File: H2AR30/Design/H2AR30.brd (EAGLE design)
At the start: 34.6 x 30 mm, 59 parts, among them P1 HEXABIT_17.32, U2 INA199A2DCKT, U3 INA199A2DCKT, U4 TEXAS_INSTRUMENTS_REF3212AIDB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, X1 XTALL_CSTCE8M00G52

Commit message: some bugs fixed
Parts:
- U2, U3: value INA199A2DCKT -> INA199B2DCKT
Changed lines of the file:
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@@
 <attribute name="VALUE" x="6.26" y="-27.758" size="1.016" layer="27"/>
 </element>
-<element name="U2" library="HEXABITZ_ICs" library_urn="urn:adsk.eagle:library:20064554" package="SOT65P210X110-6N" package3d_urn="urn:adsk.eagle:package:19904117/2" value="INA199A2DCKT" x="9.906" y="-32.512" smashed="yes">
+<element name="U2" library="HEXABITZ_ICs" library_urn="urn:adsk.eagle:library:20064554" package="SOT65P210X110-6N" package3d_urn="urn:adsk.eagle:package:19904117/2" value="INA199B2DCKT" x="9.906" y="-32.512" smashed="yes">
 <attribute name="DESCRIPTION" value="26V, bi-directional current sense amplifier 6-SC70 -40 to 125" x="9.906" y="-32.512" size="1.778" layer="27" display="off"/>
 <attribute name="MFN" value="Texas Instruments" x="9.906" y="-32.512" size="1.778" layer="27" display="off"/>
-<attribute name="MPN" value="INA199A2DCKT" x="9.906" y="-32.512" size="1.778" layer="27" display="off"/>
+<attribute name="MPN" value="INA199B2DCKT" x="9.906" y="-32.512" size="1.778" layer="27" display="off"/>
 <attribute name="NAME" x="6.4516" y="-29.972" size="2.0828" layer="25" ratio="10" rot="SR0"/>
-<attribute name="OCTOPART_URL" value="https://octopart.com/ina199a2dckt-texas+instruments-18607270?r=sp" x="9.906" y="-32.512" size="1.778" layer="27" display="off"/>
+<attribute name="OCTOPART_URL" value="https://octopart.com/ina199b2dckt-texas+instruments-24258237?r=sp" x="9.906" y="-32.512" size="1.778" layer="27" display="off"/>
 <attribute name="VALUE" x="6.4516" y="-36.957" size="2.0828" layer="27" ratio="10" rot="SR0"/>
 </element>
@@
 <attribute name="VALUE" x="6.985" y="-108.839" size="1.27" layer="27"/>
 </element>
-<element name="U3" library="HEXABITZ_ICs" library_urn="urn:adsk.eagle:library:20064554" package="SOT65P210X110-6N" package3d_urn="urn:adsk.eagle:package:19904117/2" value="INA199A2DCKT" x="9.906" y="-112.903" smashed="yes">
+<element name="U3" library="HEXABITZ_ICs" library_urn="urn:adsk.eagle:library:20064554" package="SOT65P210X110-6N" package3d_urn="urn:adsk.eagle:package:19904117/2" value="INA199B2DCKT" x="9.906" y="-112.903" smashed="yes">
 <attribute name="DESCRIPTION" value="26V, bi-directional current sense amplifier 6-SC70 -40 to 125" x="9.906" y="-112.903" size="1.778" layer="27" display="off"/>
 <attribute name="MFN" value="Texas Instruments" x="9.906" y="-112.903" size="1.778" layer="27" display="off"/>
-<attribute name="MPN" value="INA199A2DCKT" x="9.906" y="-112.903" size="1.778" layer="27" display="off"/>
+<attribute name="MPN" value="INA199B2DCKT" x="9.906" y="-112.903" size="1.778" layer="27" display="off"/>
 <attribute name="NAME" x="6.4516" y="-110.363" size="2.0828" layer="25" ratio="10" rot="SR0"/>
-<attribute name="OCTOPART_URL" value="https://octopart.com/ina199a2dckt-texas+instruments-18607270?r=sp" x="9.906" y="-112.903" size="1.778" layer="27" display="off"/>
+<attribute name="OCTOPART_URL" value="https://octopart.com/ina199b2dckt-texas+instruments-24258237?r=sp" x="9.906" y="-112.903" size="1.778" layer="27" display="off"/>
 <attribute name="VALUE" x="6.4516" y="-117.348" size="2.0828" layer="27" ratio="10" rot="SR0"/>
 </element>

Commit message: some fixes
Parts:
- R10, R9: value 330k -> 1M
- R8: value 330K -> 1M
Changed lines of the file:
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@@
 <attribute name="VALUE" x="6.731" y="-94.234" size="1.27" layer="27"/>
 </element>
-<element name="R8" library="HEXABITZ_RCLS" library_urn="urn:adsk.eagle:library:20064561" package="R1206" package3d_urn="urn:adsk.eagle:package:23540/2" value="330K" x="8.255" y="-97.917" smashed="yes">
+<element name="R8" library="HEXABITZ_RCLS" library_urn="urn:adsk.eagle:library:20064561" package="R1206" package3d_urn="urn:adsk.eagle:package:23540/2" value="1M" x="8.255" y="-97.917" smashed="yes">
 <attribute name="NAME" x="6.985" y="-96.647" size="1.27" layer="25"/>
 <attribute name="POPULARITY" value="19" x="8.255" y="-97.917" size="1.778" layer="27" display="off"/>
@@
 <attribute name="VALUE" x="6.985" y="-100.457" size="1.27" layer="27"/>
 </element>
-<element name="R9" library="HEXABITZ_RCLS" library_urn="urn:adsk.eagle:library:20064561" package="R1206" package3d_urn="urn:adsk.eagle:package:23540/2" value="330k" x="8.255" y="-102.108" smashed="yes">
+<element name="R9" library="HEXABITZ_RCLS" library_urn="urn:adsk.eagle:library:20064561" package="R1206" package3d_urn="urn:adsk.eagle:package:23540/2" value="1M" x="8.255" y="-102.108" smashed="yes">
 <attribute name="NAME" x="6.985" y="-100.838" size="1.27" layer="25"/>
 <attribute name="POPULARITY" value="19" x="8.255" y="-102.108" size="1.778" layer="27" display="off"/>
@@
 <attribute name="VALUE" x="6.985" y="-104.648" size="1.27" layer="27"/>
 </element>
-<element name="R10" library="HEXABITZ_RCLS" library_urn="urn:adsk.eagle:library:20064561" package="R1206" package3d_urn="urn:adsk.eagle:package:23540/2" value="330k" x="8.255" y="-106.299" smashed="yes">
+<element name="R10" library="HEXABITZ_RCLS" library_urn="urn:adsk.eagle:library:20064561" package="R1206" package3d_urn="urn:adsk.eagle:package:23540/2" value="1M" x="8.255" y="-106.299" smashed="yes">
 <attribute name="NAME" x="6.985" y="-105.029" size="1.27" layer="25"/>
 <attribute name="POPULARITY" value="19" x="8.255" y="-106.299" size="1.778" layer="27" display="off"/>

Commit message: no message
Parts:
- removed C13, C20: 1.00uF, HEXABITZ_RCLS:C-0805-POL
- P1: value HEXABIT_17.32 -> HEXABIT__NO_P1_P5_P6_P7_P12; device hexabitz_connectors:HEXABIT_17.32 -> hexabitz_connectors:HEXABIT_17.32_NO_P1_P6_P5_P7_P12
- R10, R8, R9: value 1M -> 1M0
- R11, R12, R4, R5: value 1.01R -> 1R0
- R14: value 3.3K -> 150R; device HEXABITZ_RCLS:R-0603 -> HEXABITZ_RCLS:R1206
- U3: value INA199B2DCKT -> INA199B1DCKT
- U4: value TEXAS_INSTRUMENTS_REF3212AIDBVRTEXAS_INSTRUMENTS_REF3212AIDBVR_0_0 -> TEXAS_INSTRUMENTS_REF2033AIDDCRTEXAS_INSTRUMENTS_REF2033AIDDCR_0_2; device HEXABITZ_ICs:TEXAS_INSTRUMENTS_REF3212AIDBVR_0 -> HEXABITZ_ICs:TEXAS_INSTRUMENTS_REF2033AIDDCR_2
- moved C24 207.7 mm to (34.7, 41.5), turned to 270 degrees
- moved R14 191.9 mm to (30.7, 44.5), flipped to the bottom, turned to 90 degrees
- moved C22 190.2 mm to (35.2, 33.4), turned to 270 degrees
- moved U4 186.4 mm to (34.7, 37.2), turned to 90 degrees
- moved C23 185.1 mm to (34.7, 23.7), turned to 180 degrees
- moved D3 184.1 mm to (32.0, 40.0), turned to 60 degrees
- moved R15 183.9 mm to (35.2, 30.2), turned to 270 degrees
- moved C21 162.3 mm to (27.9, 23.4), turned to 90 degrees
- moved R11 157.0 mm to (31.8, 29.6), turned to 270 degrees
- moved C18 156.4 mm to (27.9, 26.4), turned to 270 degrees
- moved R12 156.1 mm to (29.5, 29.6), turned to 270 degrees
- moved FB4 154.7 mm to (31.8, 33.3), turned to 270 degrees
- moved FB5 154.3 mm to (29.5, 33.3), turned to 270 degrees
- moved C19 153.0 mm to (24.8, 32.3), flipped to the bottom, turned to 270 degrees
- moved R10 152.9 mm to (33.7, 44.5), flipped to the bottom, turned to 90 degrees
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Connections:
- net N$13 renamed CURRENT_P
- net N$14 renamed CURRENT_N
- removed net USART1_RX: P1.PAD_PD5, U1.P$31
- removed net USART1_TX: P1.PAD_PU5, U1.P$30
- removed net USART4_RX: P1.PAD_PD1, U1.P$11
- removed net USART4_TX: P1.PAD_PU1, U1.P$10
- removed net VDDA: C1.1, C13.1, C14.1, C2.1, C20.1, C21.1, C24.1, FB1.1, U1.P$9
- removed net VSSA: C1.2, C13.2, C14.2, C2.2, C20.2, C21.2, C24.2, R2.2, U1.P$8
- net AGND: now also C1.2, C14.2, C2.2, C21.2, C24.2, R2.2, U1.P$8; no longer U4.1
- net CURRENT_SENSE: now also U1.P$17; no longer U1.P$29
- net GND: now also U1.P$2, U1.P$20, U1.P$27, U1.P$28, U1.P$3; no longer P1.PAD_PD12, P1.PAD_PD7
- net NEUTRAL: now also P2.1; no longer P2.2
- net PHASE: now also P2.2; no longer P2.1
- net USART5_RX: no longer P1.PAD_PD6
- net USART5_TX: no longer P1.PAD_PU6
- net VCC: now also C1.1, C14.1, C2.1, C21.1, C24.1, FB1.1, U1.P$9, U4.5
- net VDD: no longer P1.PAD_PU12, P1.PAD_PU7
- net VOLTAGE_SENSE: now also U1.P$29; no longer U1.P$17
- net V_REF: now also U4.1; no longer U4.5, U4.6
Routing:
- net VCC: track 0.00 -> 68.7 mm, vias 0 -> 3
- net AGND: track 0.00 -> 64.8 mm, vias 0 -> 6
- net V_REF: track 0.00 -> 22.8 mm, vias 0 -> 3
- net VDD: track 0.00 -> 18.0 mm, vias 0 -> 3
- net N$21: track 0.00 -> 16.7 mm, vias 0 -> 1
- net USART3_TX: track 0.00 -> 16.2 mm, vias 0 -> 1
- net NEUTRAL: track 0.00 -> 15.8 mm, vias 0 -> 1
- net USART3_RX: track 0.00 -> 15.8 mm
- net CT_1: track 0.00 -> 14.9 mm
- net B1: track 0.00 -> 14.4 mm, vias 0 -> 1
- net USART2_TX: track 0.00 -> 14.0 mm, vias 0 -> 1
- net USART6_TX: track 0.00 -> 13.1 mm, vias 0 -> 1
- net N$7: track 0.00 -> 13.0 mm, vias 0 -> 1
- net USART2_RX: track 0.00 -> 12.9 mm
- net N$3: track 0.00 -> 12.7 mm, vias 0 -> 1
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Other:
- board text added: "CT1"
- board text added: "CT2"
- board text added: "N"
- board text added: "PH"
- board text removed: "P1"
- board text removed: "P5"
- board text removed: "P6"

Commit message: no message
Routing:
- net N$21: track 16.7 -> 15.9 mm

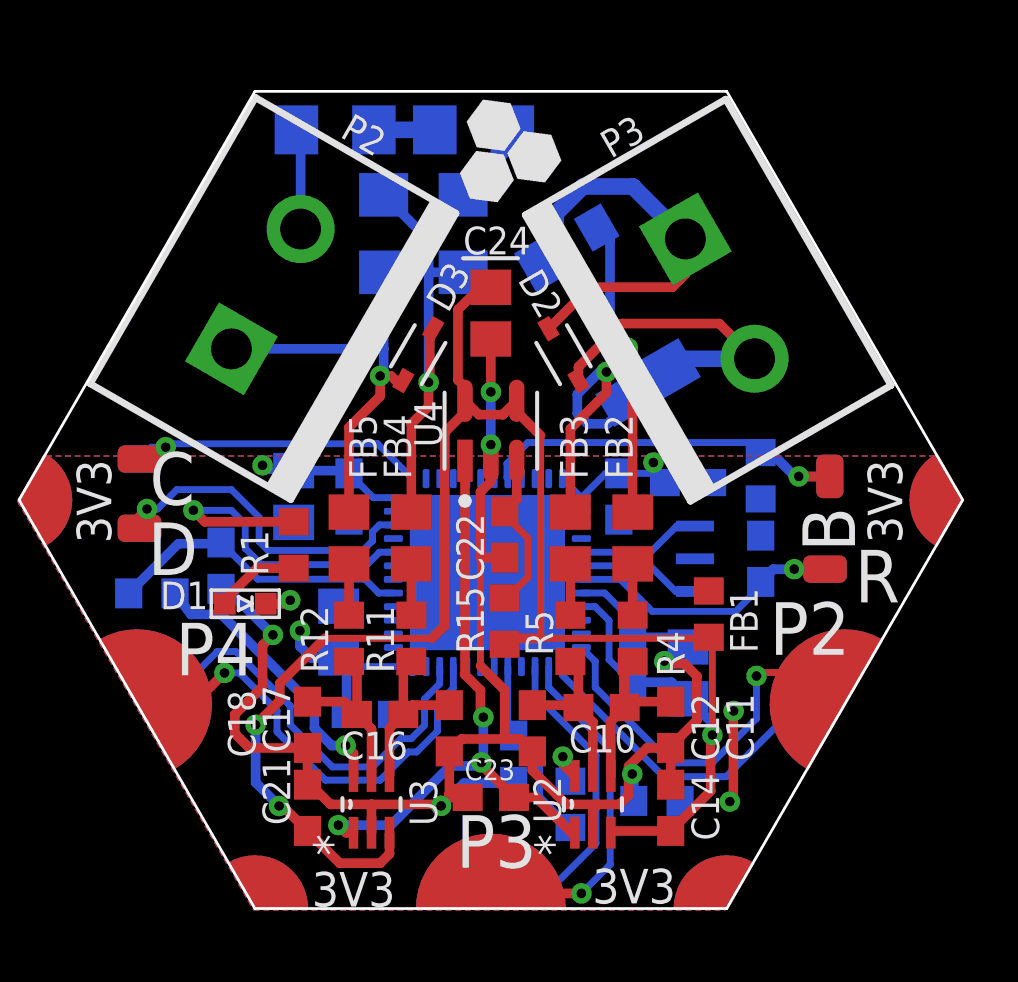
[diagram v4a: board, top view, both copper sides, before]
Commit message: Final Design: High voltage logos were added High voltage clearance checked * were added to boot pins 100A & 4A (optional ) CTs  were added to BOM ERC & DRC were made
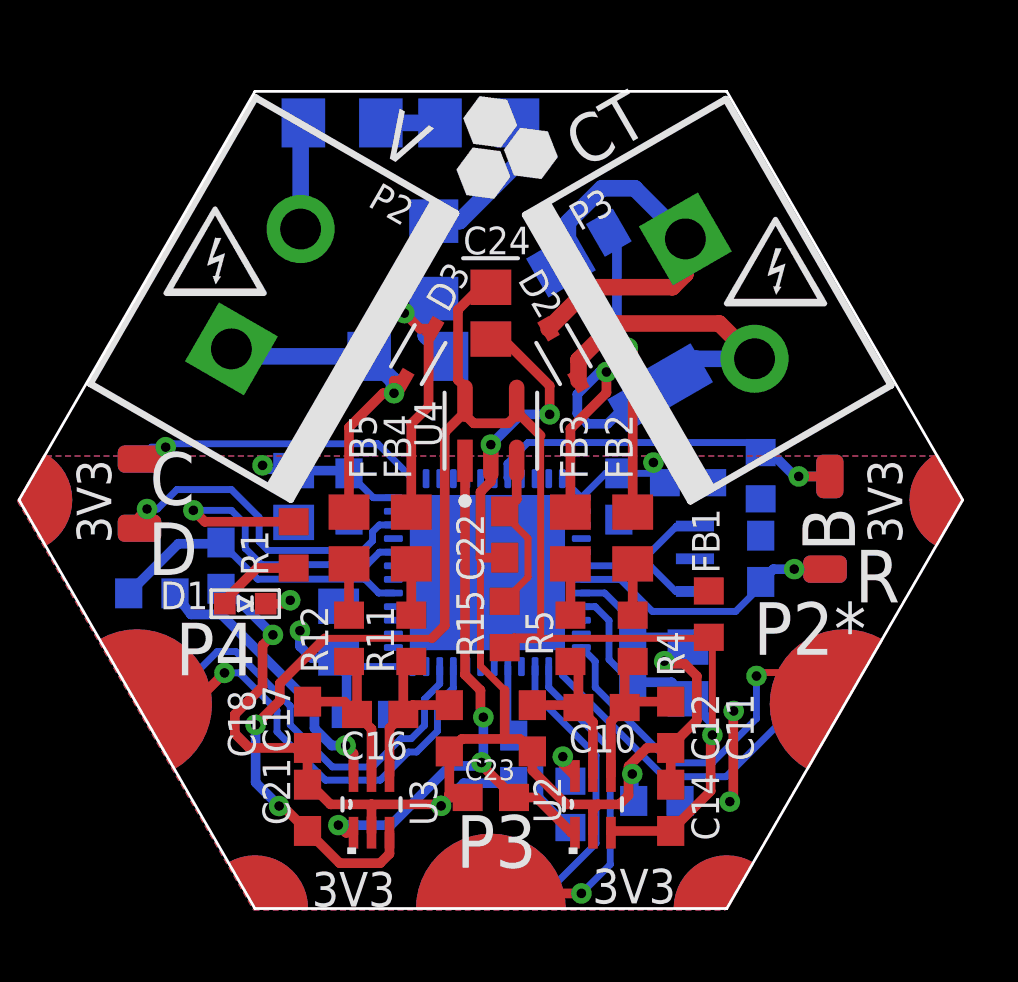
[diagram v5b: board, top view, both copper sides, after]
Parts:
- moved R14 4.60 mm to (31.6, 39.9), turned to 180 degrees
- moved R10 1.45 mm to (32.6, 43.5)
- moved R6 0.48 mm to (39.4, 41.3)
- moved R8 0.36 mm to (29.2, 48.5)
- moved R9 0.32 mm to (34.2, 48.5)
- moved R15 0.13 mm to (35.2, 30.1)
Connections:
- net USART2_RX renamed USART2*_RX
- net USART2_TX renamed USART2*_TX
- removed net USART5_RX: U1.P$40
- removed net USART5_TX: U1.P$39
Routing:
- net N$21: track 15.9 -> 12.7 mm
- net NEUTRAL: track 15.8 -> 13.0 mm
- net AGND: track 64.8 -> 67.4 mm
- net N$5: track 4.57 -> 2.03 mm
- net N$24: track 3.13 -> 5.44 mm
- net VCC: track 68.5 -> 69.4 mm
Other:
- board text added: "CT"
- board text added: "P2*"
- board text added: "V"
- board text removed: "P2"
